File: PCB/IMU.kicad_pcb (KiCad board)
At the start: 2 copper layers, 86.2 x 49.8 mm, 68 parts, among them IC1 STM32F405VGT, IC2 ADP3335ARMZ-3.3, IC3 ADP3335ARMZ-5, IC4 MS5611-01BA03, P1 UART1, P2 SWD, P3 UART2, P4 SPI, P5 BATTERY, P6 USB_OTG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

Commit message: Add deleted schematic
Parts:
- P4: footprint Connectors_Molex:Connector_Microfit3_Header_02x04_Straight_43045-0828 -> Pin_Headers:Pin_Header_Straight_2x04
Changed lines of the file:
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@@
   (general
     (links 188)
-    (no_connects 3)
-    (area 142.699999 78.199999 229.050001 128.050001)
+    (no_connects 10)
+    (area 142.699999 77.315 241.569798 130.505952)
     (thickness 1.6)
     (drawings 10)
@@
     (pad "" np_thru_hole circle (at 7.5 -2.1 180) (size 1.1 1.1) (drill 1.1) (layers *.Cu *.Mask F.SilkS))
   )
-  (module Connectors_Molex:Connector_Microfit3_Header_02x04_Straight_43045-0828 (layer F.Cu)
-    (at 148.5 103.5 180)
-    (descr "Microfit3 Header Straight 02x04 43045-0828")
-    (tags "Microfit 02x04 header straight 3mm")
-    (fp_text reference P4 (at -4 5 180) (layer F.SilkS)
-      (effects (font (size 1 1) (thickness 0.15)))
-    )
-    (fp_text value SPI (at -4 -8 180) (layer F.Fab)
-      (effects (font (size 1 1) (thickness 0.15)))
-    )
-    (fp_line (start 4.5 2.85) (end 4.5 -5.3) (layer F.CrtYd) (width 0.05))
-    (fp_line (start 4.5 2.85) (end -13.5 2.85) (layer F.CrtYd) (width 0.05))
-    (fp_line (start -13.5 2.85) (end -13.5 -5.3) (layer F.CrtYd) (width 0.05))
-    (fp_line (start 4.5 -5.3) (end -13.5 -5.3) (layer F.CrtYd) (width 0.05))
-    (fp_line (start 4.3 2.65) (end 4.3 -5.1) (layer F.SilkS) (width 0.15))
-    (fp_line (start -13.3 2.65) (end -13.3 -5.1) (layer F.SilkS) (width 0.15))
-    (fp_line (start 4.3 2.65) (end -13.3 2.65) (layer F.SilkS) (width 0.15))
-    (fp_line (start 4.3 -5.1) (end -13.3 -5.1) (layer F.SilkS) (width 0.15))
-    (pad "" np_thru_hole circle (at -12 -4 180) (size 1.1 1.1) (drill 1.1) (layers *.Cu *.Mask F.SilkS))
-    (pad 1 thru_hole circle (at 0 0 180) (size 1.6 1.6) (drill 1.1) (layers *.Cu *.Mask F.SilkS)
-      (net 86 SPI3_SCK))
-    (pad 2 thru_hole circle (at -3 0 180) (size 1.6 1.6) (drill 1.1) (layers *.Cu *.Mask F.SilkS)
-      (net 1 +3V3))
-    (pad 3 thru_hole circle (at -6 0 180) (size 1.6 1.6) (drill 1.1) (layers *.Cu *.Mask F.SilkS)
-      (net 87 SPI3_MISO))
-    (pad 4 thru_hole circle (at -9 0 180) (size 1.6 1.6) (drill 1.1) (layers *.Cu *.Mask F.SilkS)
-      (net 77 SPI3_NSS))
-    (pad 5 thru_hole circle (at 0 -3 180) (size 1.6 1.6) (drill 1.1) (layers *.Cu *.Mask F.SilkS)
-      (net 88 SPI3_MOSI))
-    (pad 6 thru_hole circle (at -3 -3 180) (size 1.6 1.6) (drill 1.1) (layers *.Cu *.Mask F.SilkS)
-      (net 45 /DATA_RDY))
-    (pad 7 thru_hole circle (at -6 -3 180) (size 1.6 1.6) (drill 1.1) (layers *.Cu *.Mask F.SilkS)
-      (net 2 GND))
-    (pad 8 thru_hole circle (at -9 -3 180) (size 1.6 1.6) (drill 1.1) (layers *.Cu *.Mask F.SilkS)
-      (net 2 GND))
-    (pad "" np_thru_hole circle (at 3 -3.94 180) (size 1.1 1.1) (drill 1.1) (layers *.Cu *.Mask F.SilkS))
-  )
   (module Measurement_Points:Measurement_Point_Round-SMD-Pad_Big (layer F.Cu)
     (at 145.5 112.5)
@@
     (pad 32 thru_hole circle (at 22.559899 -19.362802 180) (size 2.5654 2.5654) (drill 2.4892) (layers *.Cu *.Mask F.SilkS))
   )
+  (module Pin_Headers:Pin_Header_Straight_2x04 (layer F.Cu)
+    (at 148.5 103.5 180)
+    (descr "Through hole pin header")
+    (tags "pin header")
+    (fp_text reference P4 (at 0 -5.1 180) (layer F.SilkS)
+      (effects (font (size 1 1) (thickness 0.15)))
+    )
+    (fp_text value SPI (at 0 -3.1 180) (layer F.Fab)
+      (effects (font (size 1 1) (thickness 0.15)))
+    )
+    (fp_line (start -1.75 -1.75) (end -1.75 9.4) (layer F.CrtYd) (width 0.05))
+    (fp_line (start 4.3 -1.75) (end 4.3 9.4) (layer F.CrtYd) (width 0.05))
+    (fp_line (start -1.75 -1.75) (end 4.3 -1.75) (layer F.CrtYd) (width 0.05))
+    (fp_line (start -1.75 9.4) (end 4.3 9.4) (layer F.CrtYd) (width 0.05))
+    (fp_line (start -1.27 1.27) (end -1.27 8.89) (layer F.SilkS) (width 0.15))
+    (fp_line (start -1.27 8.89) (end 3.81 8.89) (layer F.SilkS) (width 0.15))
+    (fp_line (start 3.81 8.89) (end 3.81 -1.27) (layer F.SilkS) (width 0.15))
+    (fp_line (start 3.81 -1.27) (end 1.27 -1.27) (layer F.SilkS) (width 0.15))
+    (fp_line (start 0 -1.55) (end -1.55 -1.55) (layer F.SilkS) (width 0.15))
+    (fp_line (start 1.27 -1.27) (end 1.27 1.27) (layer F.SilkS) (width 0.15))
+    (fp_line (start 1.27 1.27) (end -1.27 1.27) (layer F.SilkS) (width 0.15))
+    (fp_line (start -1.55 -1.55) (end -1.55 0) (layer F.SilkS) (width 0.15))
+    (pad 1 thru_hole rect (at 0 0 180) (size 1.7272 1.7272) (drill 1.016) (layers *.Cu *.Mask F.SilkS)
+      (net 86 SPI3_SCK))
+    (pad 2 thru_hole oval (at 2.54 0 180) (size 1.7272 1.7272) (drill 1.016) (layers *.Cu *.Mask F.SilkS)
+      (net 1 +3V3))
+    (pad 3 thru_hole oval (at 0 2.54 180) (size 1.7272 1.7272) (drill 1.016) (layers *.Cu *.Mask F.SilkS)
+      (net 87 SPI3_MISO))
+    (pad 4 thru_hole oval (at 2.54 2.54 180) (size 1.7272 1.7272) (drill 1.016) (layers *.Cu *.Mask F.SilkS)
+      (net 77 SPI3_NSS))
+    (pad 5 thru_hole oval (at 0 5.08 180) (size 1.7272 1.7272) (drill 1.016) (layers *.Cu *.Mask F.SilkS)
+      (net 88 SPI3_MOSI))
+    (pad 6 thru_hole oval (at 2.54 5.08 180) (size 1.7272 1.7272) (drill 1.016) (layers *.Cu *.Mask F.SilkS)
+      (net 45 /DATA_RDY))
+    (pad 7 thru_hole oval (at 0 7.62 180) (size 1.7272 1.7272) (drill 1.016) (layers *.Cu *.Mask F.SilkS)
+      (net 2 GND))
+    (pad 8 thru_hole oval (at 2.54 7.62 180) (size 1.7272 1.7272) (drill 1.016) (layers *.Cu *.Mask F.SilkS)
+      (net 2 GND))
+    (model Pin_Headers.3dshapes/Pin_Header_Straight_2x04.wrl
+      (at (xyz 0.05 -0.15 0))
+      (scale (xyz 1 1 1))
+      (rotate (xyz 0 0 90))
+    )
+  )
   (gr_text "IMU Err" (at 225.25 122.25 90) (layer F.SilkS)

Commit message: Change SPI connector on PCB
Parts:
- moved P4 6.60 mm to (154.5, 106.2), turned to 90 degrees
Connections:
- P4 pad 1: SPI3_SCK -> GND
- P4 pad 3: SPI3_MISO -> GND
- P4 pad 5: SPI3_MOSI -> /DATA_RDY
- P4 pad 6: /DATA_RDY -> SPI3_SCK
- P4 pad 7: GND -> SPI3_MOSI
- P4 pad 8: GND -> SPI3_MISO
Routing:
- net SPI3_MOSI: track 29.7 -> 12.4 mm, vias 1 -> 0
- net SPI3_MISO: track 24.1 -> 11.8 mm, vias 1 -> 0
- net SPI3_SCK: track 26.5 -> 15.3 mm
- net /DATA_RDY: track 27.8 -> 18.6 mm
- net +3V3: track 210.1 -> 206.5 mm
- net SPI3_NSS: track 27.3 -> 28.2 mm

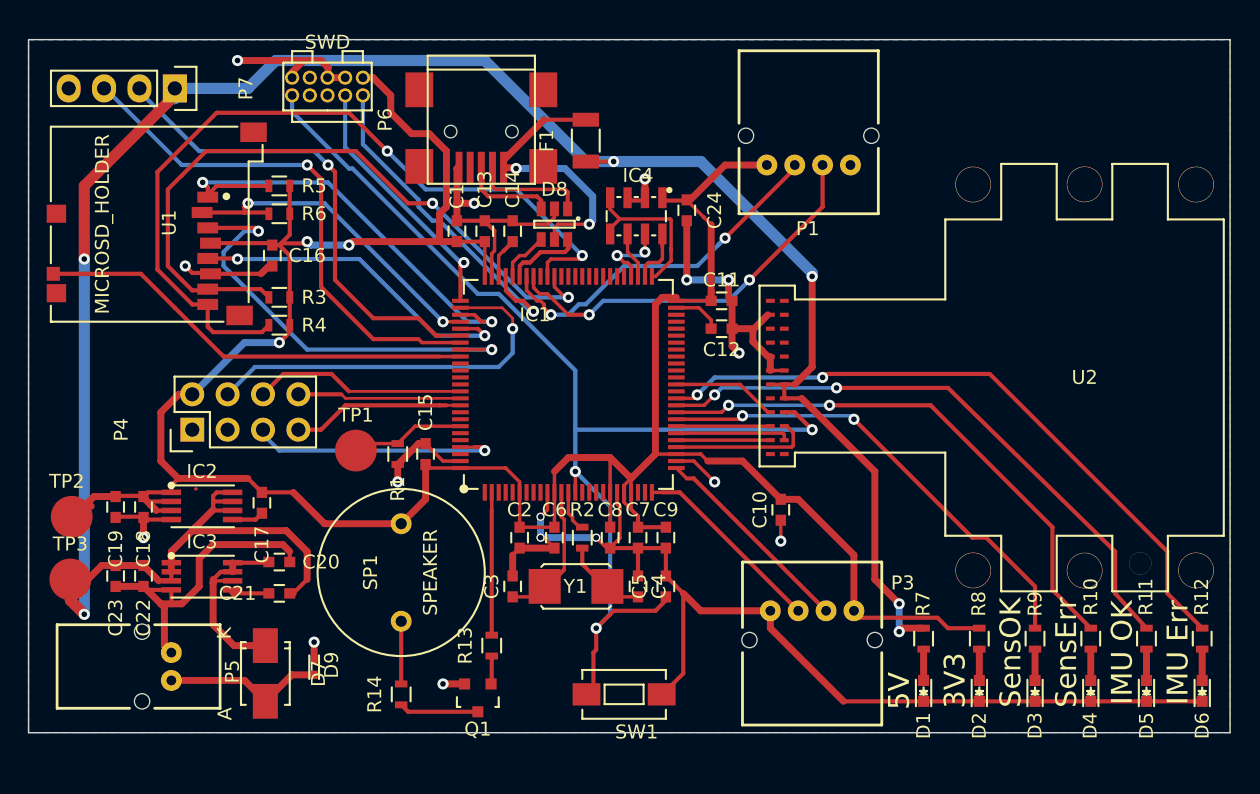
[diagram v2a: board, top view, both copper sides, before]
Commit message: Reduced number of long traces in ground plane by shuffling a number of components around. Also reduced the length of the PCB as an added bonus.
The silkscreen is currently messed up as a result of these changes - I've not had time to fix it.
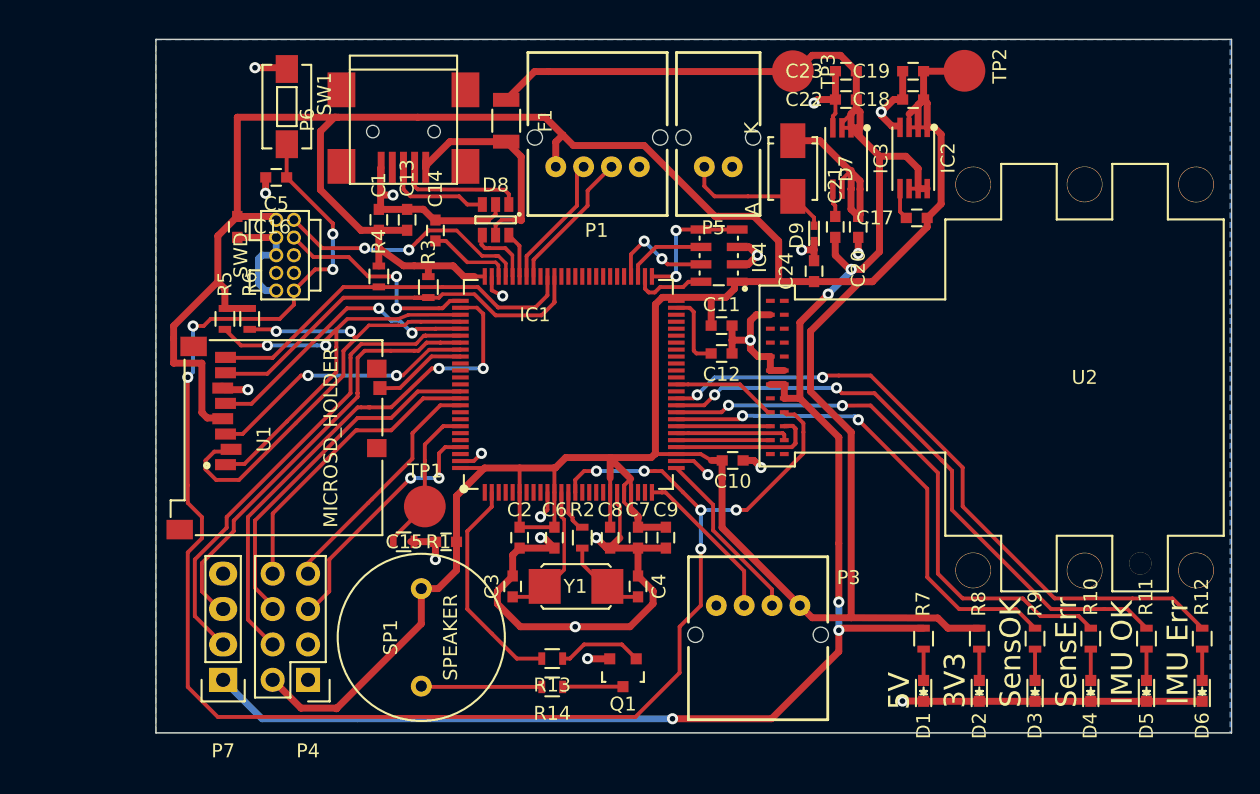
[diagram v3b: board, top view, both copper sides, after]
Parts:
- moved TP2 72.1 mm to (209.9, 80.1), turned to 270 degrees
- moved C19 65.2 mm to (206.2, 80.5), turned to 180 degrees
- moved C23 63.7 mm to (201.4, 80.5), turned to 180 degrees
- moved TP3 63.4 mm to (197.6, 80.5), turned to 270 degrees
- moved C18 62.5 mm to (206.2, 82.5), turned to 180 degrees
- moved C22 60.9 mm to (201.4, 82.5), turned to 180 degrees
- moved IC2 60.3 mm to (207.3, 84.5), turned to 270 degrees
- moved IC3 58.5 mm to (202.4, 84.6), turned to 270 degrees
- moved P5 53.1 mm to (191.3, 87.4), turned to 0 degrees
- moved D7 52.4 mm to (197.6, 87.5)
- moved C17 51.3 mm to (206.5, 91.0), turned to 180 degrees
- moved SW1 48.6 mm to (161.3, 83.1), turned to 270 degrees
- moved C20 48.0 mm to (202.3, 91.7), turned to 270 degrees
- moved C21 47.8 mm to (200.7, 91.7), turned to 90 degrees
- moved D9 46.8 mm to (199.1, 92.7), turned to 90 degrees
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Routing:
- net +3V3: track 206.5 -> 290.2 mm, vias 3 -> 0
- net GND: track 180.9 -> 129.8 mm, vias 16 -> 21
- net ~RST: track 81.3 -> 123.8 mm, vias 3 -> 9
- net SDIO_D1: track 58.2 -> 27.6 mm, vias 2 -> 0
- net /SDCard/CARD_DETECT: track 31.7 -> 6.75 mm
- net +5V: track 165.8 -> 144.0 mm, vias 6 -> 5
- net SDIO_D0: track 50.1 -> 30.1 mm, vias 2 -> 0
- net USART1_TX: track 28.8 -> 10.2 mm, vias 2 -> 0
- net USART1_RX: track 26.8 -> 9.57 mm, vias 2 -> 0
- net SDIO_CMD: track 31.8 -> 19.5 mm
- net SDIO_D3: track 24.4 -> 35.4 mm
- net SPI3_SCK: track 15.3 -> 25.5 mm
- net SPI3_MISO: track 11.8 -> 21.2 mm
- net SPI3_NSS: track 28.2 -> 37.1 mm, vias 1 -> 2
- net /SWDIO: track 24.6 -> 18.6 mm, vias 1 -> 2
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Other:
- board size 86.2 x 49.8 mm -> 77.2 x 49.8 mm
- net class Default: trace_width 0.25 -> 0.28

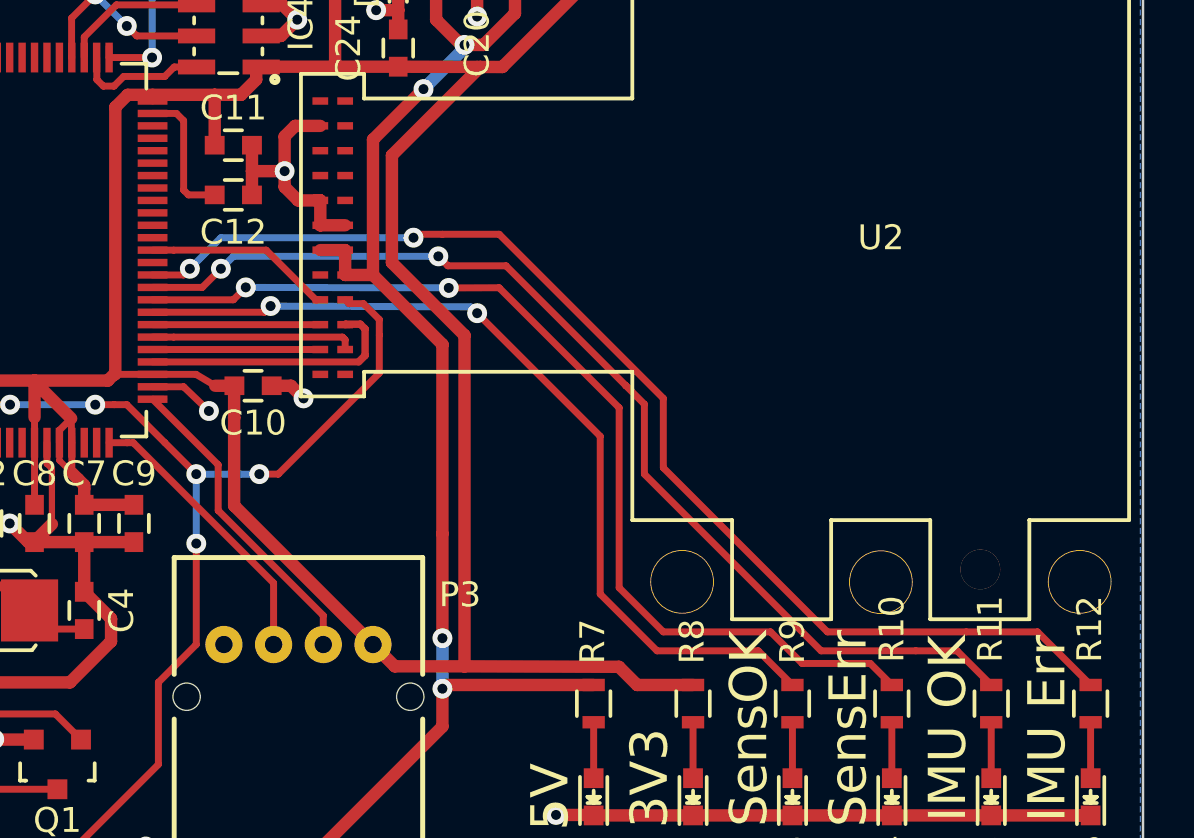
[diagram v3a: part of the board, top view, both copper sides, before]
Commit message: Altered the pinout to make the PCB somewhat cleaner.
The changed pins are:

nIMU moved to pin 40
IMU moved to pin 39
nSensors moved to pin 38
Sensors moved to pin 37
ADIS IRQ moved to pin 34
SPI1_NSS moved to pin 33
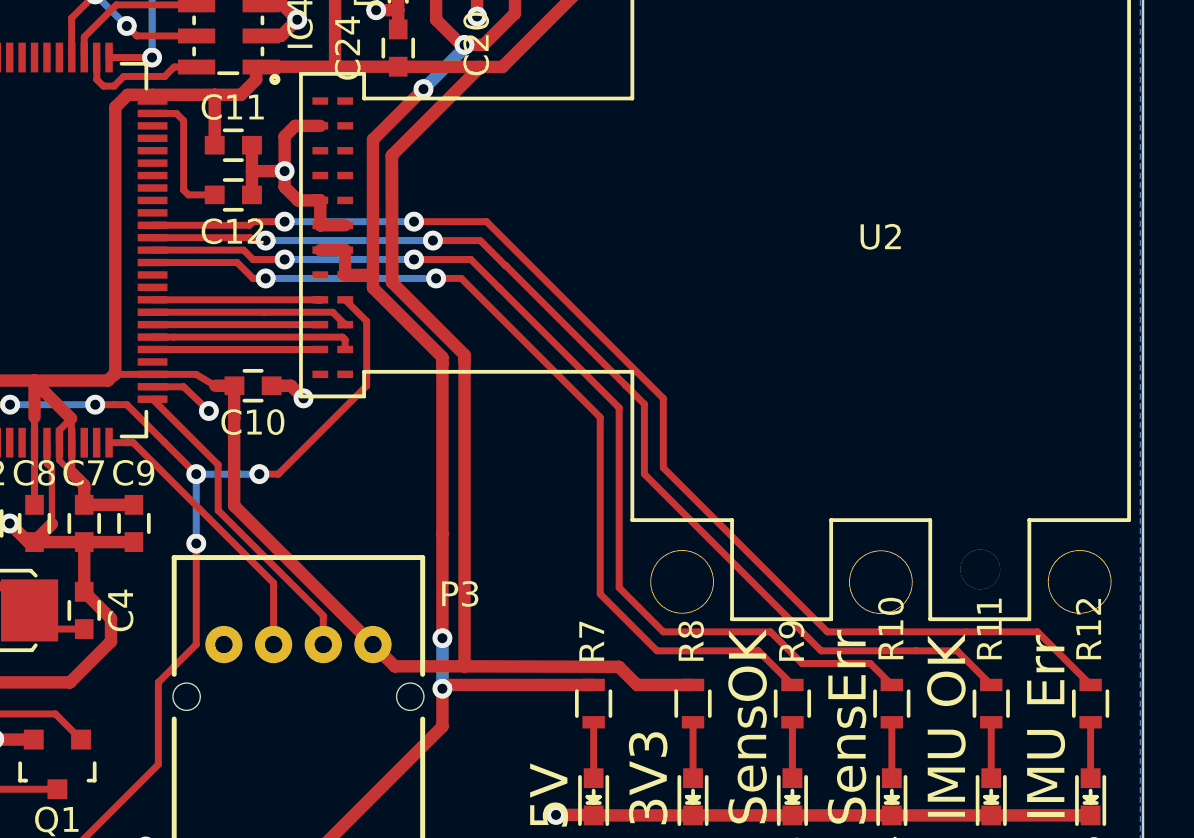
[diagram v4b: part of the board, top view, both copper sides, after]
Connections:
- IC1 pad 29: SPI1_NSS -> Net-(IC1-Pad29)
- IC1 pad 33: /StatusIndicators/Sensors -> SPI1_NSS
- IC1 pad 34: /StatusIndicators/~Sensors -> /IntertialSensors/IRQ
- IC1 pad 35: /StatusIndicators/IMU -> Net-(IC1-Pad35)
- IC1 pad 36: /StatusIndicators/~IMU -> Net-(IC1-Pad36)
- IC1 pad 37: Net-(IC1-Pad37) -> /StatusIndicators/Sensors
- IC1 pad 38: /IntertialSensors/IRQ -> /StatusIndicators/~Sensors
- IC1 pad 39: Net-(IC1-Pad39) -> /StatusIndicators/IMU
- IC1 pad 40: Net-(IC1-Pad40) -> /StatusIndicators/~IMU
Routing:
- net +3V3: track 290.2 -> 295.3 mm
- net SPI1_NSS: track 10.8 -> 8.16 mm
- net /StatusIndicators/Sensors: track 35.9 -> 37.2 mm
- net ~RST: track 123.8 -> 123.1 mm
- net /IntertialSensors/IRQ: track 7.58 -> 6.96 mm
